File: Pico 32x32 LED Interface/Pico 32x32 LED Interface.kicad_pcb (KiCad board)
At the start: 2 copper layers, 2 parts, among them J1001 Conn_01x20_Female, U1001 SN74LVC4245APWR

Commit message: Working on things...
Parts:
- added C1001: 100n, Capacitor_SMD:C_0402_1005Metric, F.Cu at (102.9, 67.3)
- added C1002: 100n, Capacitor_SMD:C_0402_1005Metric, F.Cu at (110.5, 67.3)
- added J1002: Conn_02x08_Odd_Even, Connector_PinHeader_2.54mm:PinHeader_2x08_P2.54mm_Vertical, F.Cu at (82.5, 76.2)
- U1001: footprint Package_SO:TSSOP-24_4.4x6.5mm_P0.5mm -> Package_SO:TSSOP-24_6.1x7.8mm_P0.65mm
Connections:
- U1001 pad 1: Net-(U1001-Pad1) -> +5V
- U1001 pad 11: Net-(U1001-Pad11) -> GND
- U1001 pad 12: Net-(U1001-Pad12) -> GND
- U1001 pad 13: Net-(U1001-Pad13) -> GND
- U1001 pad 2: Net-(U1001-Pad2) -> GND
- U1001 pad 22: Net-(U1001-Pad22) -> GND
- U1001 pad 23: Net-(U1001-Pad23) -> +3V3
- U1001 pad 24: Net-(U1001-Pad24) -> +3V3

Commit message: Finishing draft
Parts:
- removed J1001: Conn_01x20_Female, Connector_PinHeader_2.54mm:PinHeader_1x20_P2.54mm_Vertical
- added C2: 100n, Capacitor_SMD:C_0402_1005Metric, F.Cu at (115.6, 88.9)
- added C4: 100n, Capacitor_SMD:C_0402_1005Metric, F.Cu at (123.2, 88.9)
- added U2: SN74LVC4245APWR, Package_SO:TSSOP-24_6.1x7.8mm_P0.65mm, F.Cu at (119.4, 94.0)
- added U3: Pico_Header, Pico 32x32 LED Interface:Pico_In_Headers, F.Cu at (142.2, 86.4)
- moved J1 21.6 mm to (104.1, 77.5)
- moved C3 14.2 mm to (123.2, 73.7)
- moved C1 14.2 mm to (115.6, 73.7)
- moved U1 14.2 mm to (119.4, 78.7)
- renumbered C1001 to C1, C1002 to C3, J1002 to J1, U1001 to U1
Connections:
- J1 pad 13: /CLK -> /CLKOut
- U1 pad 10: Net-(U1001-Pad10) -> /G2Out
- U1 pad 3: Net-(U1001-Pad3) -> /CLKOut
- U1 pad 4: Net-(U1001-Pad4) -> /LatchOut
- U1 pad 5: Net-(U1001-Pad5) -> /B2Out
- U1 pad 6: Net-(U1001-Pad6) -> /R2Out
- U1 pad 7: Net-(U1001-Pad7) -> /B1Out
- U1 pad 8: Net-(U1001-Pad8) -> /R1Out
- U1 pad 9: Net-(U1001-Pad9) -> /G1Out
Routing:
- net +3V3: track 0.00 -> 85.1 mm, vias 0 -> 4
- net /CLKOut: track 0.00 -> 50.2 mm
- net /LatchOut: track 0.00 -> 45.9 mm
- net GND: track 0.00 -> 35.3 mm, vias 0 -> 6
- net /B2Out: track 0.00 -> 35.1 mm
- net /R2Out: track 0.00 -> 31.1 mm
- net /B1Out: track 0.00 -> 27.1 mm
- net /~OEOut: track 0.00 -> 26.5 mm
- net Net-(U1-Pad21): track 0.00 -> 24.6 mm
- net Net-(U1-Pad20): track 0.00 -> 22.6 mm
- net Net-(U1-Pad19): track 0.00 -> 18.3 mm
- net /AOut: track 0.00 -> 16.7 mm
- net /R1Out: track 0.00 -> 16.5 mm
- net Net-(U1-Pad18): track 0.00 -> 16.4 mm
- net Net-(U2-Pad20): track 0.00 -> 15.2 mm
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- added copper zone on B.Cu, net +5V
- added copper zone on F.Cu, net GND
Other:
- board outline added: 66 x 61 mm
- board text added: "32x32 LED Array Driver"
- board text added: "A"
- board text added: "A/GP9"
- board text added: "B"
- board text added: "B/GP10"
- board text added: "B1"
- board text added: "B1/GP4"
- board text added: "B2"
- board text added: "B2/GP2"
- board text added: "C"
- board text added: "C/GP11"
- board text added: "CLK"
- board text added: "CLK/GP0"
- board text added: "D"
- board text added: "D/GP12"
- board text added: "G1"
- board text added: "G1/GP6"
- board text added: "G2"
- board text added: "G2/GP7"
- board text added: "Latch"
- board text added: "Latch/GP1"
- board text added: "R1"
- board text added: "R1/GP5"
- board text added: "R2"
- board text added: "R2/GP3"
- board text added: "RGE2021"
- board text added: "~OE"
- board text added: "~OE/GP8"

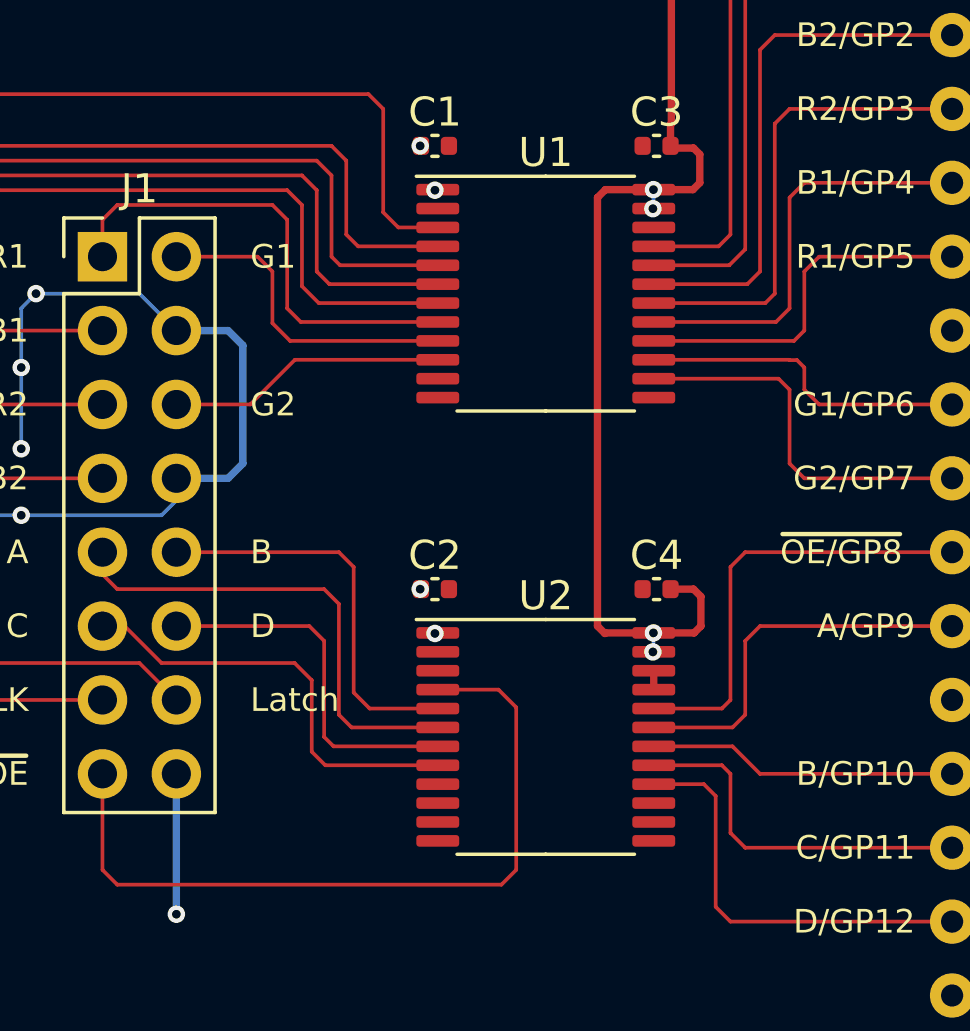
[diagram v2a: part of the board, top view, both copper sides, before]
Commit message: Fixing TSSOP footprints (#9)
Fixes the footprints of the TSSOP packages, after JLCPCB caught the error.

Since order, I've noticed two more issues:
- The decoupling capacitors may need larger footprints too (there was a warning about them, but JLCPCB didn't message me like they did for the TSSOP footprints)
- The pinout from the Pico needs to change. I've been learning about the differences between `out`, `set` and `sideset` pins since the order went into production
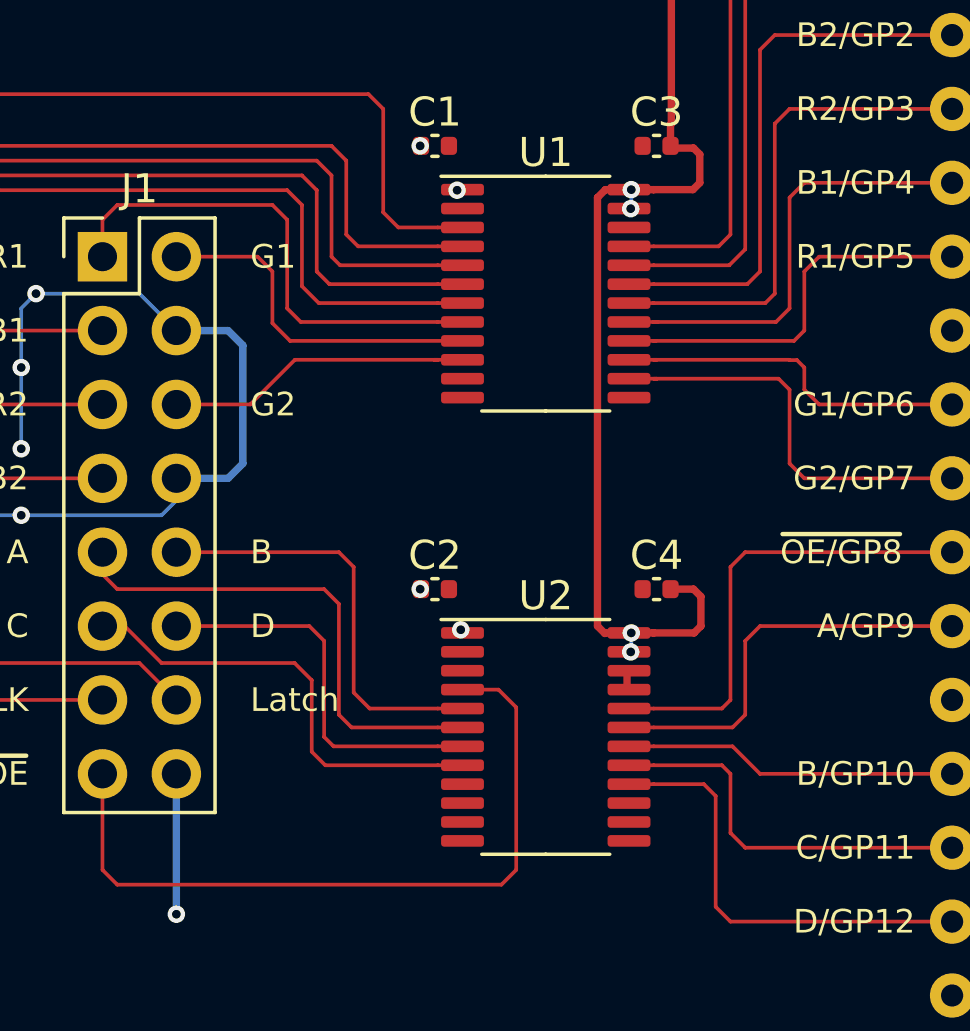
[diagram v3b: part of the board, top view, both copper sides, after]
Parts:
- U1, U2: footprint Package_SO:TSSOP-24_6.1x7.8mm_P0.65mm -> Package_SO:TSSOP-24_4.4x7.8mm_P0.65mm
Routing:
- net Net-(U1-Pad17): track 14.5 -> 15.5 mm
- net /G2Out: track 9.62 -> 10.6 mm
- net Net-(U1-Pad14): track 13.2 -> 14.1 mm
- net Net-(U1-Pad15): track 11.3 -> 12.3 mm
- net Net-(U1-Pad16): track 12.6 -> 13.6 mm
- net Net-(U2-Pad20): track 15.2 -> 16.0 mm
- net Net-(U2-Pad19): track 13.2 -> 14.0 mm
- net Net-(U2-Pad18): track 10.6 -> 11.5 mm
- net Net-(U2-Pad17): track 12.6 -> 13.5 mm
- net Net-(U2-Pad16): track 14.4 -> 15.3 mm
- net Net-(U1-Pad21): track 24.6 -> 25.5 mm
- net Net-(U1-Pad20): track 22.6 -> 23.5 mm
- net Net-(U1-Pad19): track 18.3 -> 19.1 mm
- net Net-(U1-Pad18): track 16.4 -> 17.3 mm
- net /~OEOut: track 26.5 -> 25.6 mm
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
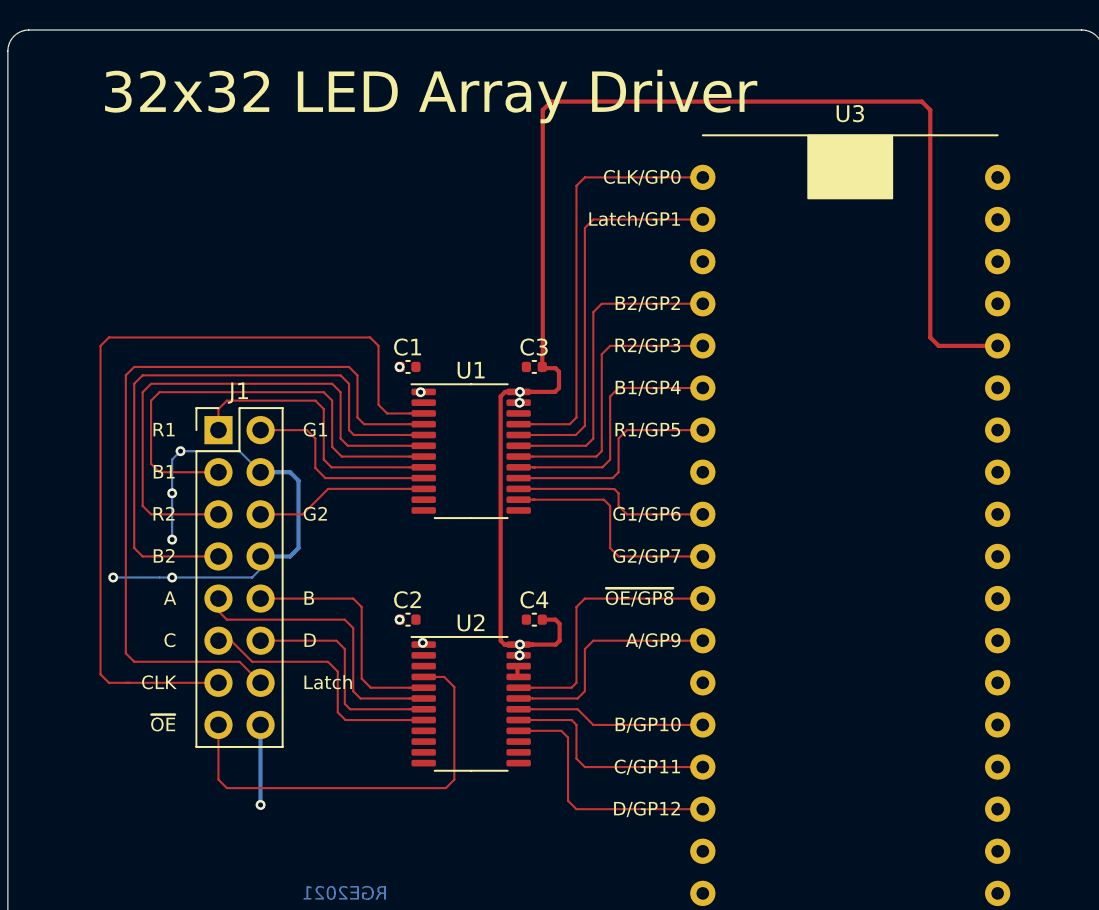
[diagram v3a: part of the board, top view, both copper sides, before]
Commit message: Working on reordering connections
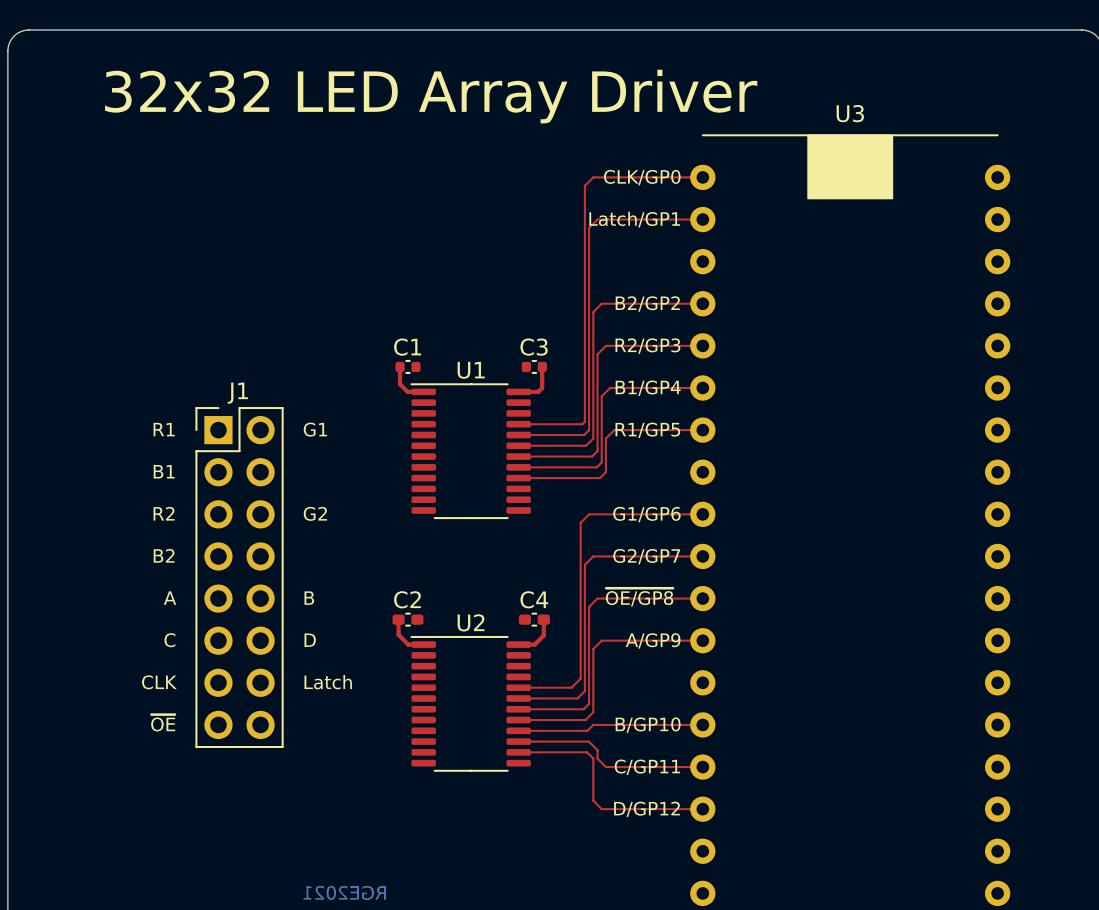
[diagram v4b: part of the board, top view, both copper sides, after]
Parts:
- C2, C4: footprint Capacitor_SMD:C_0402_1005Metric -> Capacitor_SMD:C_0402_1005Metric_Pad0.74x0.62mm_HandSolder
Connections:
- U1 pad 10: /G2Out -> Net-(U1-Pad10)
- U1 pad 3: /CLKOut -> /R1Out
- U1 pad 4: /LatchOut -> /R2Out
- U1 pad 5: /B2Out -> /B1Out
- U1 pad 6: /R2Out -> /B2Out
- U1 pad 7: /B1Out -> /G1Out
- U1 pad 8: /R1Out -> /G2Out
- U1 pad 9: /G1Out -> Net-(U1-Pad9)
- U2 pad 10: Net-(U2-Pad10) -> /~OEOut
- U2 pad 14: GND -> Net-(U2-Pad14)
- U2 pad 15: GND -> Net-(U2-Pad15)
- U2 pad 4: /~OEOut -> /COut
- U2 pad 8: /COut -> /CLKOut
- U2 pad 9: Net-(U2-Pad9) -> /LatchOut
- U3 pad 10: Net-(U1-Pad14) -> Net-(U2-Pad19)
- U3 pad 11: Net-(U2-Pad20) -> Net-(U2-Pad18)
- U3 pad 12: Net-(U2-Pad19) -> Net-(U2-Pad17)
- U3 pad 14: Net-(U2-Pad18) -> Net-(U2-Pad16)
- U3 pad 15: Net-(U2-Pad17) -> Net-(U2-Pad15)
- U3 pad 16: Net-(U2-Pad16) -> Net-(U2-Pad14)
- U3 pad 9: Net-(U1-Pad15) -> Net-(U2-Pad20)
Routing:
- net +3V3: track 85.1 -> 5.49 mm, vias 4 -> 0
- net /CLKOut: track 51.1 -> 0.00 mm
- net /LatchOut: track 46.7 -> 0.00 mm
- net /B2Out: track 36.0 -> 0.00 mm
- net GND: track 35.3 -> 0.00 mm, vias 6 -> 0
- net /R2Out: track 32.0 -> 0.00 mm
- net /B1Out: track 28.0 -> 0.00 mm
- net /~OEOut: track 25.6 -> 0.00 mm
- net /AOut: track 17.6 -> 0.00 mm
- net /R1Out: track 17.3 -> 0.00 mm
- net /COut: track 15.8 -> 0.00 mm
- net /BOut: track 14.6 -> 0.00 mm
- net Net-(U1-Pad14): track 14.1 -> 0.00 mm
- net Net-(U2-Pad14): track 0.00 -> 14.0 mm
- net /DOut: track 13.5 -> 0.00 mm
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
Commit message: Some more routine
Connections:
- U1 pad 14: Net-(U1-Pad14) -> GND
- U1 pad 15: Net-(U1-Pad15) -> GND
- U2 pad 10: /~OEOut -> /CLKOut
- U2 pad 8: /CLKOut -> /LatchOut
- U2 pad 9: /LatchOut -> /~OEOut
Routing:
- net /R2Out: track 0.00 -> 33.5 mm, vias 0 -> 1
- net /B2Out: track 0.00 -> 32.3 mm, vias 0 -> 1
- net /B1Out: track 0.00 -> 27.5 mm, vias 0 -> 1
- net /CLKOut: track 0.00 -> 26.4 mm
- net /R1Out: track 0.00 -> 21.4 mm, vias 0 -> 1
- net /~OEOut: track 0.00 -> 18.8 mm
- net /G2Out: track 0.00 -> 12.1 mm
- net /LatchOut: track 0.00 -> 11.5 mm
- net /G1Out: track 0.00 -> 10.8 mm
- net +5V: vias 0 -> 2
- net +3V3: vias 0 -> 2
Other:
- board text added: "32x32 LED Driver v2"
- board text removed: "32x32 LED Array Driver"

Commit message: Thinking a little about power
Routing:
- net +3V3: track 5.49 -> 57.7 mm
- added copper zone on B.Cu, net +3V3
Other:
- board text added: "B1/GP2"
- board text added: "B2/GP3"
- board text added: "CLK/GP12"
- board text added: "G1/GP4"
- board text added: "G2/GP5"
- board text added: "LATCH/GP10"
- board text added: "R1/GP0"
- board text added: "R2/GP1"
- board text added: "~OE/GP11"
- board text removed: "B/GP10"
- board text removed: "B1/GP4"
- board text removed: "B2/GP2"
- board text removed: "C/GP11"
- board text removed: "CLK/GP0"
- board text removed: "D/GP12"
- board text removed: "Latch/GP1"
- board text removed: "R1/GP5"
- board text removed: "R2/GP3"

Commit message: Rethinking sideset pins slightly
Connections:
- U2 pad 8: /LatchOut -> /~OEOut
- U2 pad 9: /~OEOut -> /LatchOut
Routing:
- net /CLKOut: track 26.4 -> 0.00 mm
- net /~OEOut: track 18.8 -> 0.00 mm
- net /LatchOut: track 11.5 -> 0.00 mm
